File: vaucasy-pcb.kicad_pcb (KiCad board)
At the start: 2 copper layers, 113 parts, among them J1 USB_C, J2 OLED_128x32, J3 OLED_128x64, J4 Trackball, J5 HC-05 BT, J6 DEBUG, SW1 SW_SPDT, SW2 SW_Push, SW3 RotaryEncoder_Switch, U1 STM32F401RET6, U2 USBLC6-2SC6, U3 XC6206, U4 TRRS, U5 TRRS, Y1 8MHz

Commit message: Left side finished
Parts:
- removed D32: Diode, ScottoKeebs_Components:Diode_SOD-123
- removed J3: OLED_128x64, ScottoKeebs_Components:OLED_128x64
- removed R11, R12, R15, R16: 4.7k, Resistor_SMD:R_0402_1005Metric
- removed R5: 10k, Resistor_SMD:R_0402_1005Metric
- removed S32: Keyswitch, ScottoKeebs_Hotswap:Hotswap_Choc_V1V2_1.00u
- removed U5: TRRS, ScottoKeebs_Components:TRRS_PJ-320A
- added C17: 100n, Capacitor_SMD:C_0402_1005Metric, F.Cu at (157.3, 65.9)
- C16, D1, D10, D11, D12, D13, D14, D15, D16, D17, D18, D19, D2, D20, D21, D22, D23, D24, D25, D26, D27, D28, D29, D3, D30, D31, D33, D4, D5, D6, D7, D8, D9, R6: moved to B.Cu
- J5: footprint Connector_PinHeader_2.54mm:PinHeader_1x06_P2.54mm_Vertical -> Connector_PinSocket_2.54mm:PinSocket_1x06_P2.54mm_Horizontal; moved to B.Cu
- R2: value 10k -> 100R
- SW2: footprint Button_Switch_SMD:SW_Push_1P1T_XKB_TS-1187A -> ScottoKeebs_Components:Button_TL3342
- moved S7 142.3 mm to (143.5, 48.4)
- moved S8 121.3 mm to (125.9, 119.8), turned to -15 degrees
- moved D31 120.9 mm to (161.9, 148.0), turned to 90 degrees
- moved S6 119.7 mm to (125.5, 44.9)
- moved S16 115.2 mm to (145.2, 128.0), turned to -30 degrees
- moved U4 111.7 mm to (173.5, 33.0), turned to 0 degrees
- moved S14 105.3 mm to (125.5, 61.9)
- moved D20 103.7 mm to (59.5, 102.8), turned to 90 degrees
- moved S31 98.3 mm to (161.8, 140.6), turned to -45 degrees
- moved S5 98.2 mm to (107.5, 39.4)
- moved D16 97.9 mm to (147.4, 135.0), turned to 90 degrees
- moved D18 96.9 mm to (41.5, 102.7), turned to 90 degrees
- moved D19 93.7 mm to (59.5, 85.8), turned to 90 degrees
- moved F1 93.4 mm to (159.4, 45.4), turned to -90 degrees
- moved C9 91.8 mm to (167.8, 49.4)
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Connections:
- net /MCU_VCAP1 renamed /LMCU_VCAP1
- net BT_EN renamed LBT_EN
- net ENCODER_A renamed LENCODER_A
- net ENCODER_B renamed LENCODER_B
- net OLED_SCL renamed LOLED_SCL
- net OLED_SDA renamed LOLED_SDA
- net OSC_IN renamed LOSC_IN
- net OSC_OUT renamed LOSC_OUT
- net SWCLK renamed LSWCLK
- net SWDIO renamed LSWDIO
- net TRACK_INT renamed LTRACK_INT
- net TRACK_SCL renamed LTRACK_SCL
- net TRACK_SDA renamed LTRACK_SDA
- net UART1_RX renamed LUART1_RX
- net UART1_TX renamed LUART1_TX
- net UART2_RX renamed LUART2_RX
- net UART2_TX renamed LUART2_TX
- C14 pad 2: GND -> Net-(C14-Pad2)
- C15 pad 1: GND -> Net-(C15-Pad1)
- C16 pad 1: ENCODER_PUSH -> LColumn 3
- C7 pad 2: /MCU_NRST -> LNRST
- D1 pad 1: Row 0 -> LRow 0
- D10 pad 1: Row 1 -> LRow 1
- D11 pad 1: Row 1 -> LRow 1
- D12 pad 1: Row 1 -> LRow 1
- D13 pad 1: Row 1 -> LRow 1
- D14 pad 1: Row 1 -> LRow 1
- D15 pad 1: Row 1 -> LRow 1
- D16 pad 1: Row 1 -> LROW4
- D17 pad 1: Row 2 -> LRow 2
- D18 pad 1: Row 3 -> LRow 3
- D19 pad 1: Row 2 -> LRow 2
- D2 pad 1: Row 0 -> LRow 0
- D20 pad 1: Row 3 -> LRow 3
- D21 pad 1: Row 2 -> LRow 2
- D22 pad 1: Row 3 -> LRow 3
- D23 pad 1: Row 2 -> LRow 2
- D24 pad 1: Row 3 -> LRow 3
- D25 pad 1: Row 2 -> LRow 2
- D26 pad 1: Row 3 -> LRow 3
- D27 pad 1: Row 2 -> LRow 2
- D28 pad 1: Row 3 -> LRow 3
- D29 pad 1: Row 2 -> LRow 2
- D3 pad 1: Row 0 -> LRow 0
- D30 pad 1: Row 3 -> LRow 3
- D31 pad 1: Row 2 -> LROW4
- D33 pad 1: GND -> LRow 4
- D4 pad 1: Row 0 -> LRow 0
- D5 pad 1: Row 0 -> LRow 0
- D6 pad 1: Row 0 -> LRow 0
- D7 pad 1: Row 0 -> LRow 0
- D8 pad 1: Row 0 -> LROW4
- D9 pad 1: Row 1 -> LRow 1
- J1 pad A6: D+ -> LD+
- J1 pad A7: D- -> LD-
- J1 pad B6: D+ -> LD+
- J1 pad B7: D- -> LD-
- J5 pad 5: +5V -> +3.3V
- R1 pad 2: BOOT0 -> LBOOT0
- R2 pad 1: BOOT0 -> LNRST
- R2 pad 2: GND -> Net-(R2-Pad2)
- R6 pad 1: ENCODER_PUSH -> LColumn 3
- R7 pad 1: GND -> Net-(C14-Pad2)
- R8 pad 2: GND -> Net-(C15-Pad1)
- S1 pad 1: Column 0 -> LColumn 0
- S10 pad 1: Column 1 -> LColumn 1
- S11 pad 1: Column 2 -> LColumn 2
- S12 pad 1: Column 3 -> LColumn 3
- S13 pad 1: Column 4 -> LColumn 4
- S14 pad 1: Column 5 -> LColumn 5
- S15 pad 1: Column 6 -> LColumn 6
- S16 pad 1: Column 7 -> LColumn 5
- S17 pad 1: Column 0 -> LColumn 0
- S18 pad 1: Column 0 -> LColumn 0
- S19 pad 1: Column 1 -> LColumn 1
- S2 pad 1: Column 1 -> LColumn 1
- S20 pad 1: Column 1 -> LColumn 1
- S21 pad 1: Column 2 -> LColumn 2
- S22 pad 1: Column 2 -> LColumn 2
- S23 pad 1: Column 3 -> LColumn 3
- S24 pad 1: Column 3 -> LColumn 3
- S25 pad 1: Column 4 -> LColumn 4
- S26 pad 1: Column 4 -> LColumn 4
- S27 pad 1: Column 5 -> LColumn 5
- S28 pad 1: Column 5 -> LColumn 5
- S29 pad 1: Column 6 -> LColumn 6
- S3 pad 1: Column 2 -> LColumn 2
- S30 pad 1: Column 6 -> LColumn 6
- S31 pad 1: Column 7 -> LColumn 6
- S4 pad 1: Column 3 -> LColumn 3
- S5 pad 1: Column 4 -> LColumn 4
- S6 pad 1: Column 5 -> LColumn 5
- S7 pad 1: Column 6 -> LColumn 6
- S8 pad 1: Column 7 -> LColumn 4
- S9 pad 1: Column 0 -> LColumn 0
- SW2 pad 1: +3.3V -> GND
- SW2 pad 2: BOOT0 -> Net-(R2-Pad2)
- SW3 pad A: GND -> Net-(C15-Pad1)
- SW3 pad B: GND -> Net-(C14-Pad2)
- U1 pad 10: Column 2 -> LRow 4
- U1 pad 11: Column 3 -> unconnected-(U1-PC3-Pad11)
- U1 pad 2: Row 1 -> unconnected-(U1-PC13-Pad2)
- U1 pad 20: unconnected-(U1-PA4-Pad20) -> LRow 3
- U1 pad 21: unconnected-(U1-PA5-Pad21) -> LColumn 6
- U1 pad 22: unconnected-(U1-PA6-Pad22) -> LColumn 5
- U1 pad 23: unconnected-(U1-PA7-Pad23) -> LColumn 4
- U1 pad 24: Column 4 -> unconnected-(U1-PC4-Pad24)
- U1 pad 25: Column 5 -> unconnected-(U1-PC5-Pad25)
- U1 pad 28: unconnected-(U1-PB2-Pad28) -> LColumn 0
- U1 pad 29: MCU_SDA -> LRow 0
- U1 pad 3: Row 2 -> unconnected-(U1-PC14-Pad3)
- U1 pad 36: ENCODER_PUSH -> unconnected-(U1-PB15-Pad36)
- U1 pad 37: Column 6 -> unconnected-(U1-PC6-Pad37)
- U1 pad 38: Column 7 -> unconnected-(U1-PC7-Pad38)
- U1 pad 4: Row 3 -> unconnected-(U1-PC15-Pad4)
- U1 pad 44: D- -> LsD-
- U1 pad 45: D+ -> LsD+
- U1 pad 53: Row 0 -> LColumn 1
- U1 pad 54: unconnected-(U1-PD2-Pad54) -> LRow 1
- U1 pad 55: MCU_SCL -> LColumn 2
- U1 pad 56: unconnected-(U1-PB4-Pad56) -> LColumn 3
- U1 pad 57: unconnected-(U1-PB5-Pad57) -> LRow 2
- U1 pad 60: BOOT0 -> LBOOT0
- U1 pad 7: /MCU_NRST -> LNRST
- U1 pad 8: Column 0 -> unconnected-(U1-PC0-Pad8)
- U1 pad 9: Column 1 -> unconnected-(U1-PC1-Pad9)
- U2 pad 1: D+ -> LD-
- U2 pad 3: D- -> LD+
- U2 pad 4: D- -> LsD+
- U2 pad 6: D+ -> LsD-
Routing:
- net LColumn 0: track 0.00 -> 200.7 mm, vias 0 -> 1
- net LColumn 3: track 0.00 -> 183.6 mm, vias 0 -> 9
- net LColumn 4: track 0.00 -> 181.3 mm, vias 0 -> 9
- net LColumn 1: track 0.00 -> 181.1 mm, vias 0 -> 7
- net +3.3V: track 0.00 -> 169.8 mm, vias 0 -> 11
- net LColumn 2: track 0.00 -> 167.6 mm, vias 0 -> 7
- net LRow 3: track 0.00 -> 167.1 mm, vias 0 -> 1
- net LColumn 5: track 0.00 -> 162.9 mm, vias 0 -> 9
- net LColumn 6: track 0.00 -> 161.3 mm, vias 0 -> 9
- net LRow 2: track 0.00 -> 145.2 mm, vias 0 -> 1
- net LRow 0: track 0.00 -> 139.6 mm, vias 0 -> 1
- net LRow 1: track 0.00 -> 131.0 mm, vias 0 -> 1
- net LENCODER_A: track 0.00 -> 120.8 mm, vias 0 -> 4
- net LENCODER_B: track 0.00 -> 109.5 mm, vias 0 -> 2
- net LRow 4: track 0.00 -> 97.2 mm, vias 0 -> 1
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- added copper zone on B.Cu, net GND
- added copper zone on F.Cu, net GND
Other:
- board outline added: 153.2 x 136.5 mm

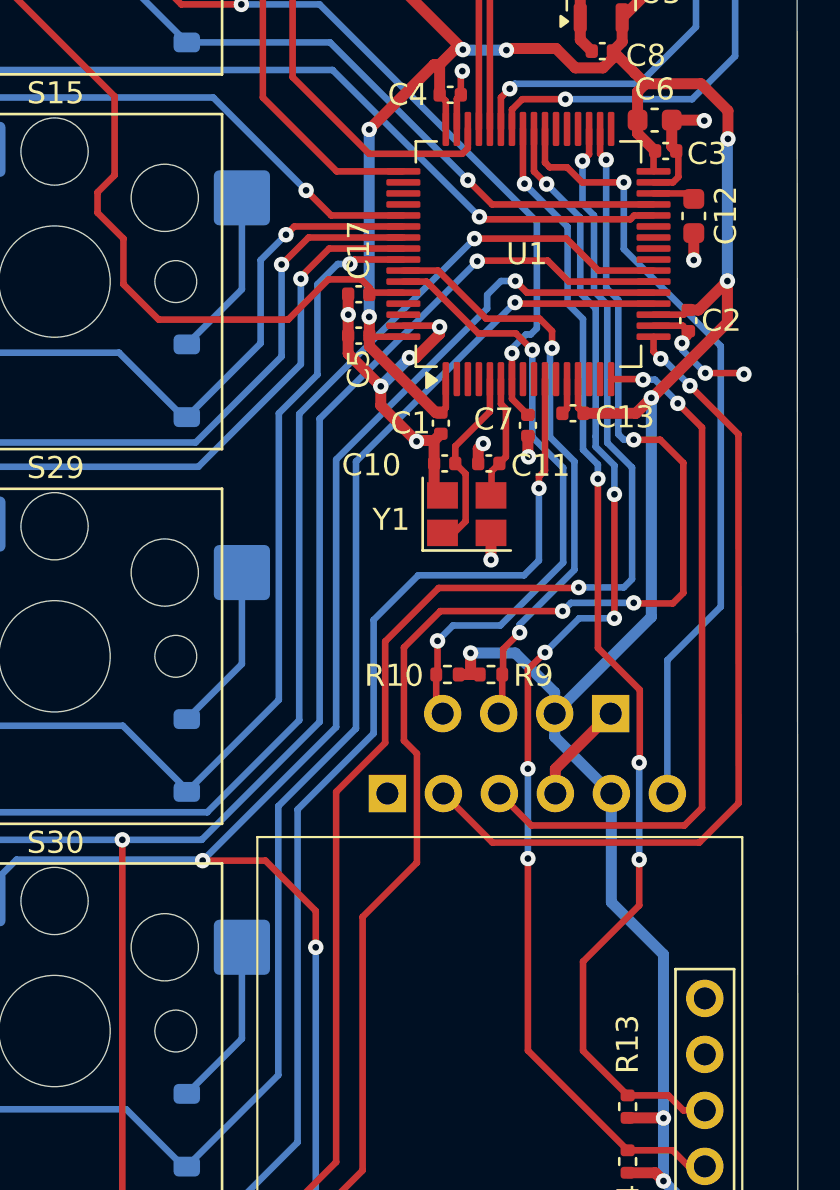
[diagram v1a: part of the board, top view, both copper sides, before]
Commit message: Track_INT added
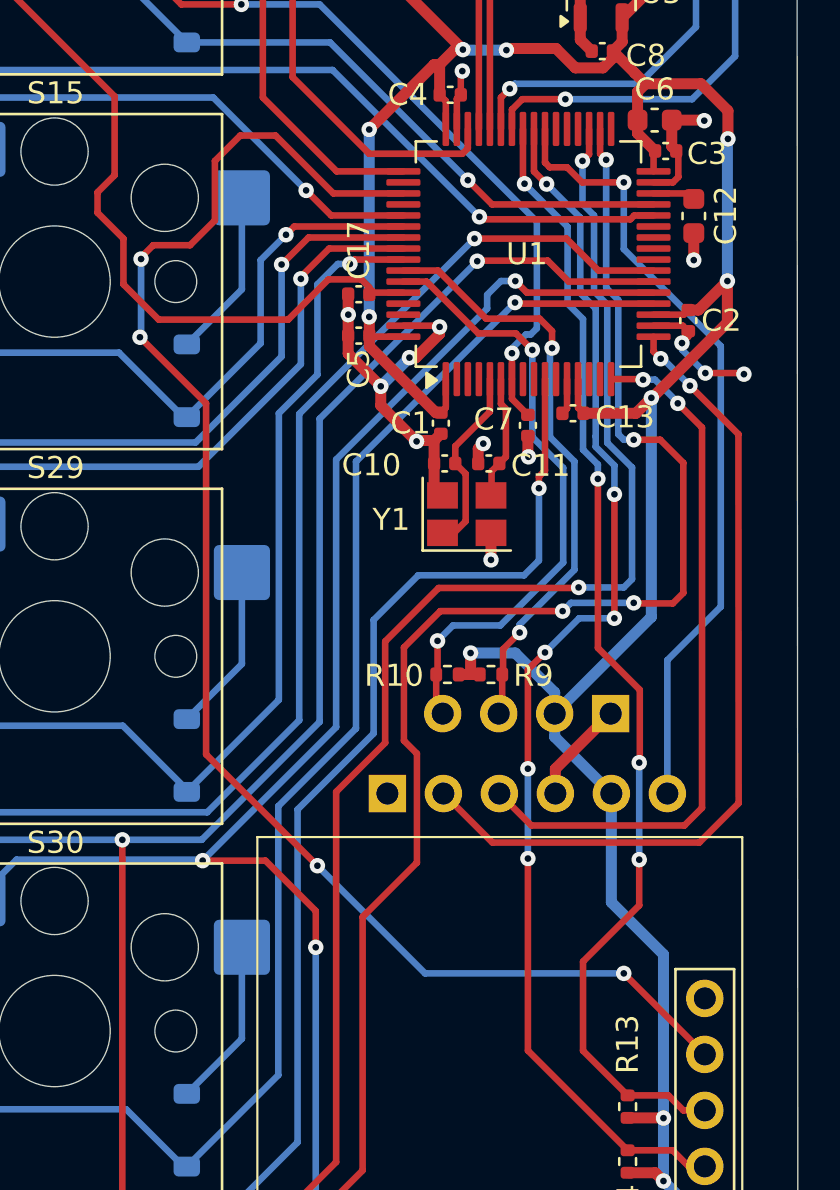
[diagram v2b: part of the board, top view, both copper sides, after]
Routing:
- net LTRACK_INT: track 0.00 -> 68.9 mm, vias 0 -> 4
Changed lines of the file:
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@@
+	)
+	(segment
+		(start 147.975 63.7)
+		(end 147.425 64.25)
+		(width 0.3)
+		(layer "F.Cu")
+		(net 83)
+	)
+	(segment
+		(start 147.375 67.875)
+		(end 150.375 70.875)
+		(width 0.3)
+		(layer "F.Cu")
+		(net 83)
+	)
+	(segment
+		(start 169.325012 96.735012)
+		(end 169.325 96.735012)
+		(width 0.3)
+		(layer "F.Cu")
+		(net 83)
+	)
+	(segment
+		(start 153.525 58.725)
+		(end 151.925 58.725)
+		(width 0.3)
+		(layer "F.Cu")
+		(net 83)
+	)
+	(segment
+		(start 150.775 62.575)
+		(end 149.65 63.7)
+		(width 0.3)
+		(layer "F.Cu")
+		(net 83)
+	)
+	(segment
+		(start 150.375 70.875)
+		(end 150.375 86.8)
+		(width 0.3)
+		(layer "F.Cu")
+		(net 83)
+	)
+	(segment
+		(start 159.325 61.35)
+		(end 156.15 61.35)
+		(width 0.3)
+		(layer "F.Cu")
+		(net 83)
+	)
+	(segment
+		(start 149.65 63.7)
+		(end 147.975 63.7)
+		(width 0.3)
+		(layer "F.Cu")
+		(net 83)
+	)
+	(segment
+		(start 173 100.41)
+		(end 169.325012 96.735012)
+		(width 0.3)
+		(layer "F.Cu")
+		(net 83)
+	)
+	(segment
+		(start 147.425 64.25)
+		(end 147.425 64.325)
+		(width 0.3)
+		(layer "F.Cu")
+		(net 83)
+	)
+	(segment
+		(start 151.925 58.725)
+		(end 150.775 59.875)
+		(width 0.3)
+		(layer "F.Cu")
+		(net 83)
+	)
+	(segment
+		(start 150.375 86.8)
+		(end 155.425 91.85)
+		(width 0.3)
+		(layer "F.Cu")
+		(net 83)
+	)
+	(segment
+		(start 156.15 61.35)
+		(end 153.525 58.725)
+		(width 0.3)
+		(layer "F.Cu")
+		(net 83)
+	)
+	(segment
+		(start 150.775 59.875)
+		(end 150.775 62.575)
+		(width 0.3)
+		(layer "F.Cu")
+		(net 83)
+	)
+	(via
+		(at 169.325 96.735012)
+		(size 0.7)
+		(drill 0.3)
+		(layers "F.Cu" "B.Cu")
+		(net 83)
+	)
+	(via
+		(at 147.425 64.325)
+		(size 0.7)
+		(drill 0.3)
+		(layers "F.Cu" "B.Cu")
+		(net 83)
+	)
+	(via
+		(at 155.425 91.85)
+		(size 0.7)
+		(drill 0.3)
+		(layers "F.Cu" "B.Cu")
+		(net 83)
+	)
+	(via
+		(at 147.375 67.875)
+		(size 0.7)
+		(drill 0.3)
+		(layers "F.Cu" "B.Cu")
+		(net 83)
+	)
+	(segment
+		(start 160.310012 96.735012)
+		(end 169.325 96.735012)
+		(width 0.3)
+		(layer "B.Cu")
+		(net 83)
+	)
+	(segment
+		(start 155.425 91.85)
+		(end 160.310012 96.735012)
+		(width 0.3)
+		(layer "B.Cu")
+		(net 83)
+	)
+	(segment
+		(start 147.425 67.825)
+		(end 147.375 67.875)
+		(width 0.3)
+		(layer "B.Cu")
+		(net 83)
+	)
+	(segment
+		(start 147.425 64.325)
+		(end 147.425 67.825)
+		(width 0.3)
+		(layer "B.Cu")
+		(net 83)
 	)
 	(segment
